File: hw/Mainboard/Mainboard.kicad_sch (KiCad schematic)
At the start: 0 parts

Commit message: hw: remove bar from video signal name
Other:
- sheet MAGIC ports: added BVIDEO; removed ~{BVIDEO}
- sheet USER ports: added BVIDEO; removed ~{BVIDEO}
- sheet VIDEO ports: added BVIDEO; removed ~{BVIDEO}
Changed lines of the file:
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@@
       (effects (font (size 1.27 1.27)) (justify right))
     )
-    (pin "~{BVIDEO}" output (at 104.14 129.54 0)
+    (pin "BVIDEO" output (at 104.14 129.54 0)
       (effects (font (size 1.27 1.27)) (justify right))
     )
@@
       (effects (font (size 1.27 1.27)) (justify right))
     )
-    (pin "~{BVIDEO}" input (at 194.31 100.33 0)
+    (pin "BVIDEO" input (at 194.31 100.33 0)
       (effects (font (size 1.27 1.27)) (justify right))
     )
@@
       (effects (font (size 1.27 1.27)) (justify left))
     )
-    (pin "~{BVIDEO}" input (at 220.98 100.33 180)
-      (effects (font (size 1.27 1.27)) (justify left))
-    )
+    (pin "BVIDEO" input (at 220.98 100.33 180)
+      (effects (font (size 1.27 1.27)) (justify left))
+    )

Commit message: hw: replace ram_ce with ram_a15
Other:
- sheet CPU \ RAM ports: added A[0..15], RAM_A; removed A[0..16], RAM_A[10..11], ~{RAM_CE}
- sheet MAGIC ports: added A[0..15], RAM_A; removed A[0..16], RAM_A[10..11], ~{RAM_CE}
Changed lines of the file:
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@@
-    (stroke (width 0) (type default) (color 0 0 0 0))
-  )
-  (wire (pts (xy 66.04 96.52) (xy 78.74 96.52))
     (stroke (width 0) (type default) (color 0 0 0 0))
   )
@@
       (effects (font (size 1.27 1.27)) (justify right))
     )
-    (pin "A[0..16]" bidirectional (at 66.04 46.99 0)
-      (effects (font (size 1.27 1.27)) (justify right))
-    )
     (pin "D[0..7]" bidirectional (at 66.04 49.53 0)
       (effects (font (size 1.27 1.27)) (justify right))
@@
       (effects (font (size 1.27 1.27)) (justify right))
     )
-    (pin "~{RAM_CE}" input (at 66.04 96.52 0)
-      (effects (font (size 1.27 1.27)) (justify right))
-    )
-    (pin "RAM_A[10..11]" input (at 66.04 52.07 0)
-      (effects (font (size 1.27 1.27)) (justify right))
-    )
     (pin "~{SO}" input (at 66.04 73.66 0)
       (effects (font (size 1.27 1.27)) (justify right))
@@
     )
     (pin "~{ML}" output (at 66.04 78.74 0)
+      (effects (font (size 1.27 1.27)) (justify right))
+    )
+    (pin "RAM_A" input (at 66.04 52.07 0)
+      (effects (font (size 1.27 1.27)) (justify right))
+    )
+    (pin "A[0..15]" bidirectional (at 66.04 46.99 0)
       (effects (font (size 1.27 1.27)) (justify right))
     )
@@
       (effects (font (size 1.27 1.27)) (justify left))
     )
-    (pin "~{RAM_CE}" output (at 78.74 96.52 180)
-      (effects (font (size 1.27 1.27)) (justify left))
-    )
-    (pin "A[0..16]" bidirectional (at 78.74 46.99 180)
-      (effects (font (size 1.27 1.27)) (justify left))
-    )
     (pin "B~{VIA_CS}" output (at 104.14 91.44 0)
       (effects (font (size 1.27 1.27)) (justify right))
@@
       (effects (font (size 1.27 1.27)) (justify left))
     )
-    (pin "RAM_A[10..11]" output (at 78.74 52.07 180)
-      (effects (font (size 1.27 1.27)) (justify left))
-    )
     (pin "~{SO}" output (at 78.74 73.66 180)
       (effects (font (size 1.27 1.27)) (justify left))
@@
       (effects (font (size 1.27 1.27)) (justify left))
     )
+    (pin "A[0..15]" bidirectional (at 78.74 46.99 180)
+      (effects (font (size 1.27 1.27)) (justify left))
+    )
+    (pin "RAM_A" output (at 78.74 52.07 180)
+      (effects (font (size 1.27 1.27)) (justify left))
+    )

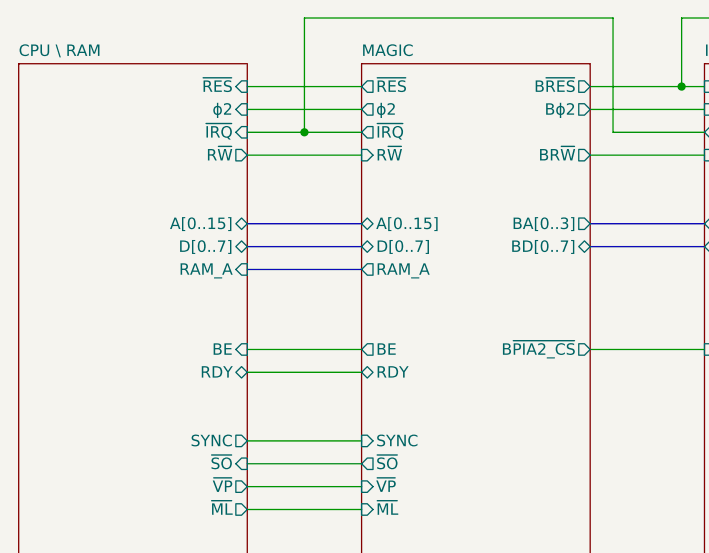
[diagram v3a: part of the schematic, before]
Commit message: hw: move DVI to separate hierarchical sheet, fix buses, annotate power
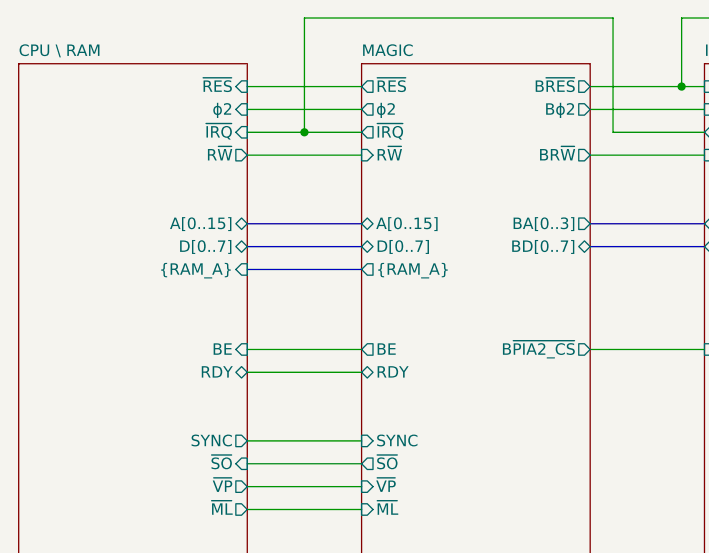
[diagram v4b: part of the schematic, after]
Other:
- sheet CPU \ RAM ports: added {RAM_A}; removed RAM_A
- sheet MAGIC ports: added {RAM_A}; removed RAM_A
